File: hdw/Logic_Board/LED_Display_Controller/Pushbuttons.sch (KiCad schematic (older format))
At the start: 21 parts, among them J1401 Encoder Ext, SW1401 Display Enable, SW1402 Brightness/Enable, U1401 MAX6816, U1402 74LVC2G14, U1403 74LVC1G79

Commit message: added ESP8266 custom footprint
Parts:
- SW1402: footprint (none) -> Electronic_Display_Footprint_Lib:ACZ11BR4E-15FA1-20C
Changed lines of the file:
@@
 F 0 "SW1402" H 1970 4750 50  0000 C CNN
 F 1 "Brightness/Enable" H 1970 4230 50  0000 C CNN
-F 2 "" H 1820 4650 50  0001 C CNN
+F 2 "Electronic_Display_Footprint_Lib:ACZ11BR4E-15FA1-20C" H 1820 4650 50  0001 C CNN
 F 3 "~" H 1970 4750 50  0001 C CNN
 	1    1970 4490

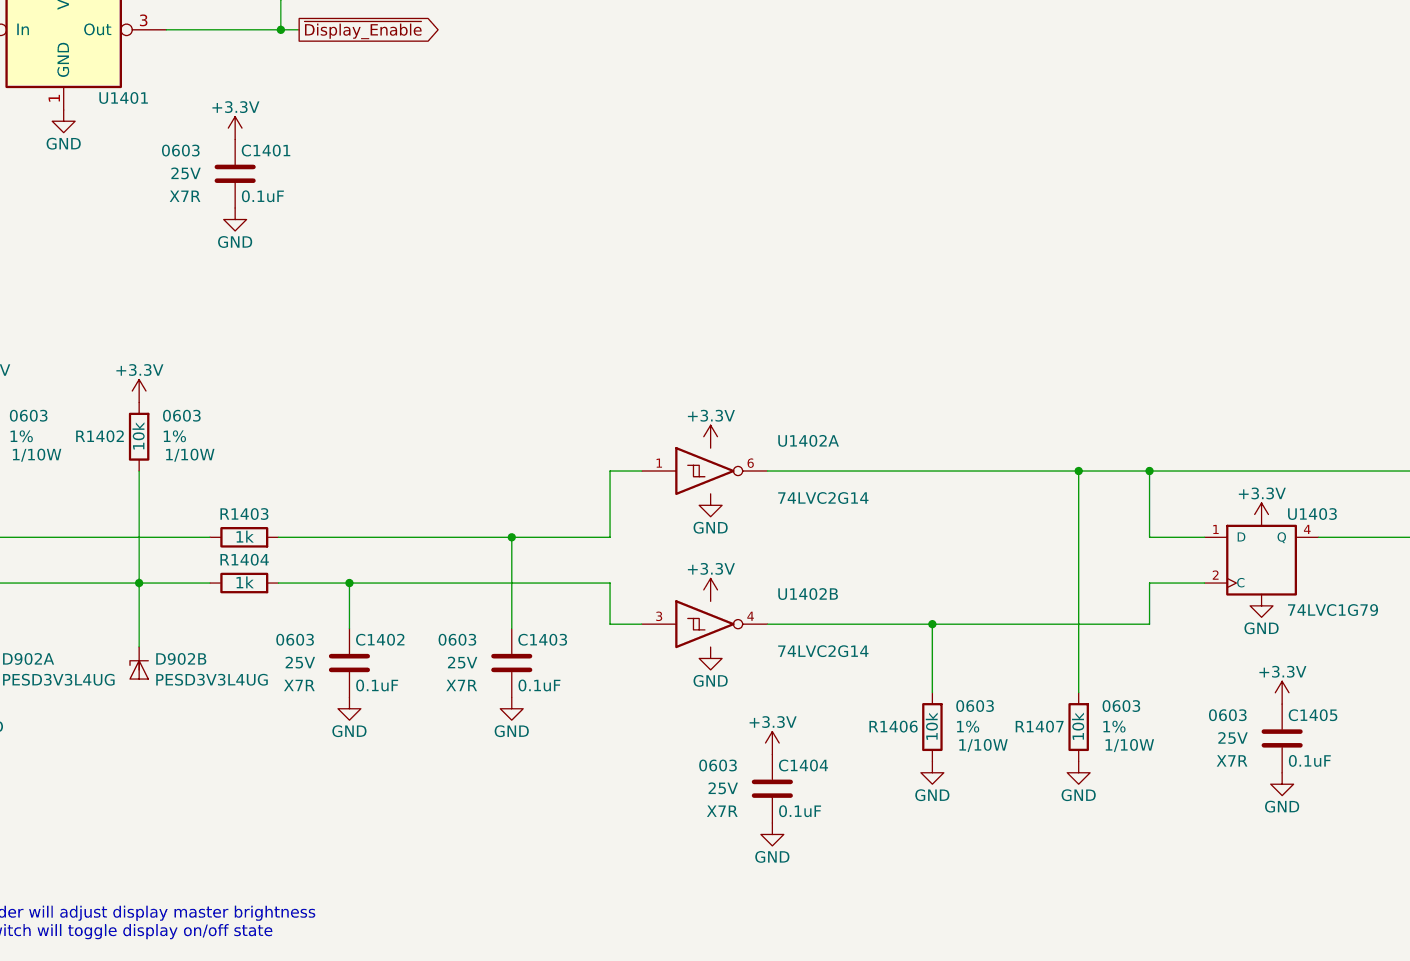
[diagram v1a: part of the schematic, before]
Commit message: Added some digikey partnumbers to components
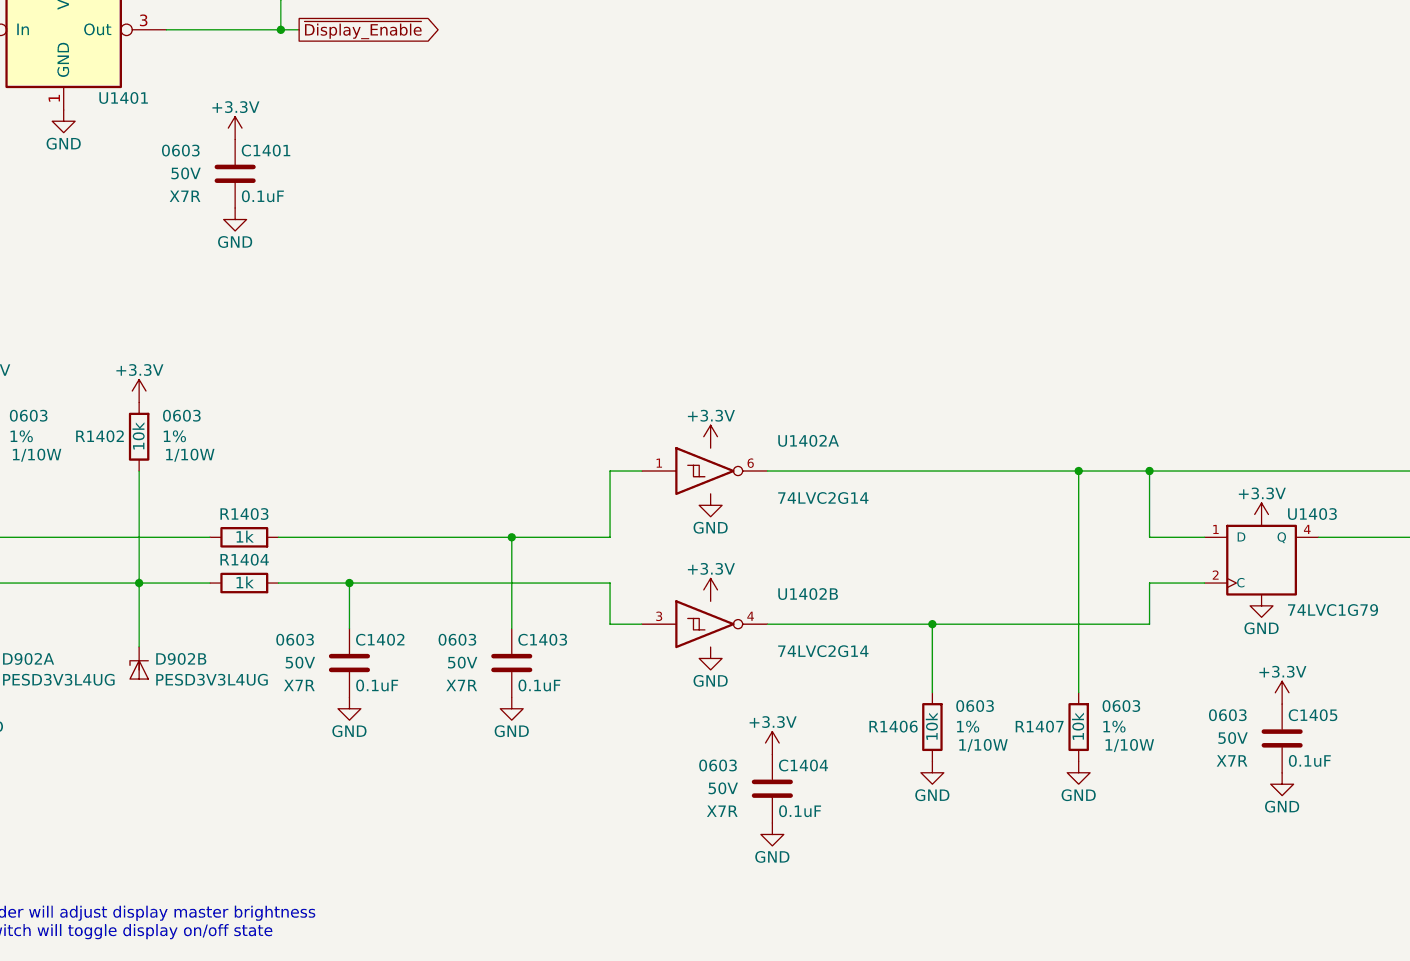
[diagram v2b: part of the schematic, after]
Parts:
- C1401, C1402, C1403, C1404, C1405: footprint (none) -> Capacitors_SMD:C_0603; Digi-Key PN PN -> 311-1344-1-ND; Voltage 25V -> 50V
- D1401, D902: Digi-Key PN (none) -> 1727-3827-1-ND
- SW1402: Digi-Key PN (none) -> 102-1753-ND
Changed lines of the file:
@@
 F 2 "Electronic_Display_Footprint_Lib:ACZ11BR4E-15FA1-20C" H 1820 4650 50  0001 C CNN
 F 3 "~" H 1970 4750 50  0001 C CNN
+F 4 "102-1753-ND" H 0   0   50  0001 C CNN "Digi-Key PN"
 	1    1970 4490
 	-1   0    0    -1
@@
 F 0 "C1401" H 4205 2900 50  0000 L CNN
 F 1 "0.1uF" H 4205 2700 50  0000 L CNN
-F 2 "" H 4218 2650 50  0001 C CNN
+F 2 "Capacitors_SMD:C_0603" H 4218 2650 50  0001 C CNN
 F 3 "" H 4205 2900 50  0001 C CNN
 F 4 "0603" H 4030 2900 50  0000 R CNN "display_footprint"
-F 5 "25V" H 4030 2800 50  0000 R CNN "Voltage"
+F 5 "50V" H 4030 2800 50  0000 R CNN "Voltage"
 F 6 "X7R" H 4030 2700 50  0000 R CNN "Dielectric"
-F 7 "PN" H 4605 3300 60  0001 C CNN "Digi-Key PN"
+F 7 "311-1344-1-ND" H 4605 3300 60  0001 C CNN "Digi-Key PN"
 	1    4180 2800
 	1    0    0    -1
@@
 F 0 "C1402" H 4705 5040 50  0000 L CNN
 F 1 "0.1uF" H 4705 4840 50  0000 L CNN
-F 2 "" H 4718 4790 50  0001 C CNN
+F 2 "Capacitors_SMD:C_0603" H 4718 4790 50  0001 C CNN
 F 3 "" H 4705 5040 50  0001 C CNN
 F 4 "0603" H 4530 5040 50  0000 R CNN "display_footprint"
-F 5 "25V" H 4530 4940 50  0000 R CNN "Voltage"
+F 5 "50V" H 4530 4940 50  0000 R CNN "Voltage"
 F 6 "X7R" H 4530 4840 50  0000 R CNN "Dielectric"
-F 7 "PN" H 5105 5440 60  0001 C CNN "Digi-Key PN"
+F 7 "311-1344-1-ND" H 5105 5440 60  0001 C CNN "Digi-Key PN"
 	1    4680 4940
 	1    0    0    -1
@@
 F 0 "C1403" H 5415 5040 50  0000 L CNN
 F 1 "0.1uF" H 5415 4840 50  0000 L CNN
-F 2 "" H 5428 4790 50  0001 C CNN
+F 2 "Capacitors_SMD:C_0603" H 5428 4790 50  0001 C CNN
 F 3 "" H 5415 5040 50  0001 C CNN
 F 4 "0603" H 5240 5040 50  0000 R CNN "display_footprint"
-F 5 "25V" H 5240 4940 50  0000 R CNN "Voltage"
+F 5 "50V" H 5240 4940 50  0000 R CNN "Voltage"
 F 6 "X7R" H 5240 4840 50  0000 R CNN "Dielectric"
-F 7 "PN" H 5815 5440 60  0001 C CNN "Digi-Key PN"
+F 7 "311-1344-1-ND" H 5815 5440 60  0001 C CNN "Digi-Key PN"
 	1    5390 4940
 	1    0    0    -1
@@
 F 0 "C1404" H 6555 5590 50  0000 L CNN
 F 1 "0.1uF" H 6555 5390 50  0000 L CNN
-F 2 "" H 6568 5340 50  0001 C CNN
+F 2 "Capacitors_SMD:C_0603" H 6568 5340 50  0001 C CNN
 F 3 "" H 6555 5590 50  0001 C CNN
 F 4 "0603" H 6380 5590 50  0000 R CNN "display_footprint"
-F 5 "25V" H 6380 5490 50  0000 R CNN "Voltage"
+F 5 "50V" H 6380 5490 50  0000 R CNN "Voltage"
 F 6 "X7R" H 6380 5390 50  0000 R CNN "Dielectric"
-F 7 "PN" H 6955 5990 60  0001 C CNN "Digi-Key PN"
+F 7 "311-1344-1-ND" H 6955 5990 60  0001 C CNN "Digi-Key PN"
 	1    6530 5490
 	1    0    0    -1
@@
 F 0 "C1405" H 8785 5370 50  0000 L CNN
 F 1 "0.1uF" H 8785 5170 50  0000 L CNN
-F 2 "" H 8798 5120 50  0001 C CNN
+F 2 "Capacitors_SMD:C_0603" H 8798 5120 50  0001 C CNN
 F 3 "" H 8785 5370 50  0001 C CNN
 F 4 "0603" H 8610 5370 50  0000 R CNN "display_footprint"
-F 5 "25V" H 8610 5270 50  0000 R CNN "Voltage"
+F 5 "50V" H 8610 5270 50  0000 R CNN "Voltage"
 F 6 "X7R" H 8610 5170 50  0000 R CNN "Dielectric"
-F 7 "PN" H 9185 5770 60  0001 C CNN "Digi-Key PN"
+F 7 "311-1344-1-ND" H 9185 5770 60  0001 C CNN "Digi-Key PN"
 	1    8760 5270
 	1    0    0    -1
@@
 F 2 "Package_TO_SOT_SMD:SOT-353_SC-70-5" H 3090 4970 50  0001 C CNN
 F 3 "http://www.nxp.com/documents/data_sheet/PESDXL4UF_G_W.pdf" H 3090 4970 50  0001 C CNN
+F 4 "1727-3827-1-ND" H 0   0   50  0001 C CNN "Digi-Key PN"
 	1    3090 4970
 	0    1    1    0
@@
 F 2 "Package_TO_SOT_SMD:SOT-353_SC-70-5" H 3760 4970 50  0001 C CNN
 F 3 "http://www.nxp.com/documents/data_sheet/PESDXL4UF_G_W.pdf" H 3760 4970 50  0001 C CNN
+F 4 "1727-3827-1-ND" H 0   0   50  0001 C CNN "Digi-Key PN"
 	2    3760 4970
 	0    1    1    0
@@
 F 2 "Package_TO_SOT_SMD:SOT-353_SC-70-5" H 2010 2420 50  0001 C CNN
 F 3 "http://www.nxp.com/documents/data_sheet/PESDXL4UF_G_W.pdf" H 2010 2420 50  0001 C CNN
+F 4 "1727-3827-1-ND" H 0   0   50  0001 C CNN "Digi-Key PN"
 	3    2010 2420
 	0    1    1    0

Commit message: Finished first pass of digikey part numbers
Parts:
- R1401, R1402, R1405, R1406, R1407, R1408: Digi-Key PN PN -> RMCF0603FT10K0CT-ND
- R1403, R1404: Digi-Key PN PN -> RMCF0603FT1K00CT-ND
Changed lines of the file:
@@
 F 5 "1%" H 4480 1890 50  0000 L CNN "Tolerance"
 F 6 "1/10W" H 4490 1810 50  0000 L CNN "Wattage"
-F 7 "PN" H 4680 2290 60  0001 C CNN "Digi-Key PN"
+F 7 "RMCF0603FT10K0CT-ND" H 4680 2290 60  0001 C CNN "Digi-Key PN"
 	1    4380 1890
 	1    0    0    -1
@@
 F 5 "1%" H 3190 3950 50  0000 L CNN "Tolerance"
 F 6 "1/10W" H 3200 3870 50  0000 L CNN "Wattage"
-F 7 "PN" H 3390 4350 60  0001 C CNN "Digi-Key PN"
+F 7 "RMCF0603FT10K0CT-ND" H 3390 4350 60  0001 C CNN "Digi-Key PN"
 	1    3090 3950
 	1    0    0    -1
@@
 F 5 "1%" H 3860 3950 50  0000 L CNN "Tolerance"
 F 6 "1/10W" H 3870 3870 50  0000 L CNN "Wattage"
-F 7 "PN" H 4060 4350 60  0001 C CNN "Digi-Key PN"
+F 7 "RMCF0603FT10K0CT-ND" H 4060 4350 60  0001 C CNN "Digi-Key PN"
 	1    3760 3950
 	1    0    0    -1
@@
 F 2 "" H 4220 4390 50  0001 C CNN
 F 3 "" H 4220 4390 50  0001 C CNN
-F 4 "PN" H 4520 4790 60  0001 C CNN "Digi-Key PN"
+F 4 "RMCF0603FT1K00CT-ND" H 4520 4790 60  0001 C CNN "Digi-Key PN"
 F 5 "0603" V 4320 4390 50  0001 C CNN "display_footprint"
 F 6 "1%" V 4420 4390 50  0001 C CNN "Tolerance"
@@
 F 2 "" H 4220 4590 50  0001 C CNN
 F 3 "" H 4220 4590 50  0001 C CNN
-F 4 "PN" H 4520 4990 60  0001 C CNN "Digi-Key PN"
+F 4 "RMCF0603FT1K00CT-ND" H 4520 4990 60  0001 C CNN "Digi-Key PN"
 F 5 "0603" V 4320 4590 50  0001 C CNN "display_footprint"
 F 6 "1%" V 4420 4590 50  0001 C CNN "Tolerance"
@@
 F 5 "1%" H 7330 5220 50  0000 L CNN "Tolerance"
 F 6 "1/10W" H 7340 5140 50  0000 L CNN "Wattage"
-F 7 "PN" H 7530 5620 60  0001 C CNN "Digi-Key PN"
+F 7 "RMCF0603FT10K0CT-ND" H 7530 5620 60  0001 C CNN "Digi-Key PN"
 	1    7230 5220
 	1    0    0    -1
@@
 F 5 "1%" H 7970 5220 50  0000 L CNN "Tolerance"
 F 6 "1/10W" H 7980 5140 50  0000 L CNN "Wattage"
-F 7 "PN" H 8170 5620 60  0001 C CNN "Digi-Key PN"
+F 7 "RMCF0603FT10K0CT-ND" H 8170 5620 60  0001 C CNN "Digi-Key PN"
 	1    7870 5220
 	1    0    0    -1
@@
 F 5 "1%" H 9700 4660 50  0000 L CNN "Tolerance"
 F 6 "1/10W" H 9710 4580 50  0000 L CNN "Wattage"
-F 7 "PN" H 9900 5060 60  0001 C CNN "Digi-Key PN"
+F 7 "RMCF0603FT10K0CT-ND" H 9900 5060 60  0001 C CNN "Digi-Key PN"
 	1    9600 4660
 	1    0    0    -1

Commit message: First pass assignment of footprints to all components
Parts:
- D1401: footprint Package_TO_SOT_SMD:SOT-353_SC-70-5 -> TO_SOT_Packages_SMD:SOT-353_SC-70-5
- J1401: footprint (none) -> Pin_Headers:Pin_Header_Straight_1x05_Pitch2.54mm
- R1401, R1402, R1403, R1404, R1405, R1406, R1407, R1408: footprint (none) -> Resistors_SMD:R_0603
- SW1401: footprint (none) -> Buttons_Switches_THT:SW_PUSH_6mm
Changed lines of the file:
@@
 F 0 "SW1401" H 1310 2455 50  0000 C CNN
 F 1 "Display Enable" H 1310 2364 50  0000 C CNN
-F 2 "" H 1310 2370 50  0001 C CNN
+F 2 "Buttons_Switches_THT:SW_PUSH_6mm" H 1310 2370 50  0001 C CNN
 F 3 "" H 1310 2370 50  0001 C CNN
 	1    1310 2170
@@
 F 0 "R1405" H 4320 1890 50  0000 R CNN
 F 1 "10k" V 4380 1890 50  0000 C CNN
-F 2 "" H 4380 1890 50  0001 C CNN
+F 2 "Resistors_SMD:R_0603" H 4380 1890 50  0001 C CNN
 F 3 "" H 4380 1890 50  0001 C CNN
 F 4 "0603" H 4480 1980 50  0000 L CNN "display_footprint"
@@
 F 0 "R1401" H 3030 3950 50  0000 R CNN
 F 1 "10k" V 3090 3950 50  0000 C CNN
-F 2 "" H 3090 3950 50  0001 C CNN
+F 2 "Resistors_SMD:R_0603" H 3090 3950 50  0001 C CNN
 F 3 "" H 3090 3950 50  0001 C CNN
 F 4 "0603" H 3190 4040 50  0000 L CNN "display_footprint"
@@
 F 0 "R1402" H 3700 3950 50  0000 R CNN
 F 1 "10k" V 3760 3950 50  0000 C CNN
-F 2 "" H 3760 3950 50  0001 C CNN
+F 2 "Resistors_SMD:R_0603" H 3760 3950 50  0001 C CNN
 F 3 "" H 3760 3950 50  0001 C CNN
 F 4 "0603" H 3860 4040 50  0000 L CNN "display_footprint"
@@
 F 0 "R1403" V 4120 4390 50  0000 C CNN
 F 1 "1k" V 4220 4390 50  0000 C CNN
-F 2 "" H 4220 4390 50  0001 C CNN
+F 2 "Resistors_SMD:R_0603" H 4220 4390 50  0001 C CNN
 F 3 "" H 4220 4390 50  0001 C CNN
 F 4 "RMCF0603FT1K00CT-ND" H 4520 4790 60  0001 C CNN "Digi-Key PN"
@@
 F 0 "R1404" V 4120 4590 50  0000 C CNN
 F 1 "1k" V 4220 4590 50  0000 C CNN
-F 2 "" H 4220 4590 50  0001 C CNN
+F 2 "Resistors_SMD:R_0603" H 4220 4590 50  0001 C CNN
 F 3 "" H 4220 4590 50  0001 C CNN
 F 4 "RMCF0603FT1K00CT-ND" H 4520 4990 60  0001 C CNN "Digi-Key PN"
@@
 F 0 "R1406" H 7170 5220 50  0000 R CNN
 F 1 "10k" V 7230 5220 50  0000 C CNN
-F 2 "" H 7230 5220 50  0001 C CNN
+F 2 "Resistors_SMD:R_0603" H 7230 5220 50  0001 C CNN
 F 3 "" H 7230 5220 50  0001 C CNN
 F 4 "0603" H 7330 5310 50  0000 L CNN "display_footprint"
@@
 F 0 "R1407" H 7810 5220 50  0000 R CNN
 F 1 "10k" V 7870 5220 50  0000 C CNN
-F 2 "" H 7870 5220 50  0001 C CNN
+F 2 "Resistors_SMD:R_0603" H 7870 5220 50  0001 C CNN
 F 3 "" H 7870 5220 50  0001 C CNN
 F 4 "0603" H 7970 5310 50  0000 L CNN "display_footprint"
@@
 F 0 "R1408" H 9540 4660 50  0000 R CNN
 F 1 "10k" V 9600 4660 50  0000 C CNN
-F 2 "" H 9600 4660 50  0001 C CNN
+F 2 "Resistors_SMD:R_0603" H 9600 4660 50  0001 C CNN
 F 3 "" H 9600 4660 50  0001 C CNN
 F 4 "0603" H 9700 4750 50  0000 L CNN "display_footprint"
@@
 F 0 "D1401" V 1964 2488 50  0000 L CNN
 F 1 "PESD3V3L4UG" V 2055 2488 50  0000 L CNN
-F 2 "Package_TO_SOT_SMD:SOT-353_SC-70-5" H 2010 2420 50  0001 C CNN
+F 2 "TO_SOT_Packages_SMD:SOT-353_SC-70-5" H 2010 2420 50  0001 C CNN
 F 3 "http://www.nxp.com/documents/data_sheet/PESDXL4UF_G_W.pdf" H 2010 2420 50  0001 C CNN
 F 4 "1727-3827-1-ND" H 0   0   50  0001 C CNN "Digi-Key PN"
@@
 F 0 "J1401" H 1110 3520 50  0000 L CNN
 F 1 "Encoder Ext" H 1120 3440 50  0000 L CNN
-F 2 "" H 1040 3530 50  0001 C CNN
+F 2 "Pin_Headers:Pin_Header_Straight_1x05_Pitch2.54mm" H 1040 3530 50  0001 C CNN
 F 3 "~" H 1040 3530 50  0001 C CNN
 	1    1040 3530

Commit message: Resolved a few library dependencies
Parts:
- D902: footprint Package_TO_SOT_SMD:SOT-353_SC-70-5 -> TO_SOT_Packages_SMD:SOT-353_SC-70-5
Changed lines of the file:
@@
 F 0 "D902" V 3044 5038 50  0000 L CNN
 F 1 "PESD3V3L4UG" V 3135 5038 50  0000 L CNN
-F 2 "Package_TO_SOT_SMD:SOT-353_SC-70-5" H 3090 4970 50  0001 C CNN
+F 2 "TO_SOT_Packages_SMD:SOT-353_SC-70-5" H 3090 4970 50  0001 C CNN
 F 3 "http://www.nxp.com/documents/data_sheet/PESDXL4UF_G_W.pdf" H 3090 4970 50  0001 C CNN
 F 4 "1727-3827-1-ND" H 0   0   50  0001 C CNN "Digi-Key PN"
@@
 F 0 "D902" V 3714 5038 50  0000 L CNN
 F 1 "PESD3V3L4UG" V 3805 5038 50  0000 L CNN
-F 2 "Package_TO_SOT_SMD:SOT-353_SC-70-5" H 3760 4970 50  0001 C CNN
+F 2 "TO_SOT_Packages_SMD:SOT-353_SC-70-5" H 3760 4970 50  0001 C CNN
 F 3 "http://www.nxp.com/documents/data_sheet/PESDXL4UF_G_W.pdf" H 3760 4970 50  0001 C CNN
 F 4 "1727-3827-1-ND" H 0   0   50  0001 C CNN "Digi-Key PN"

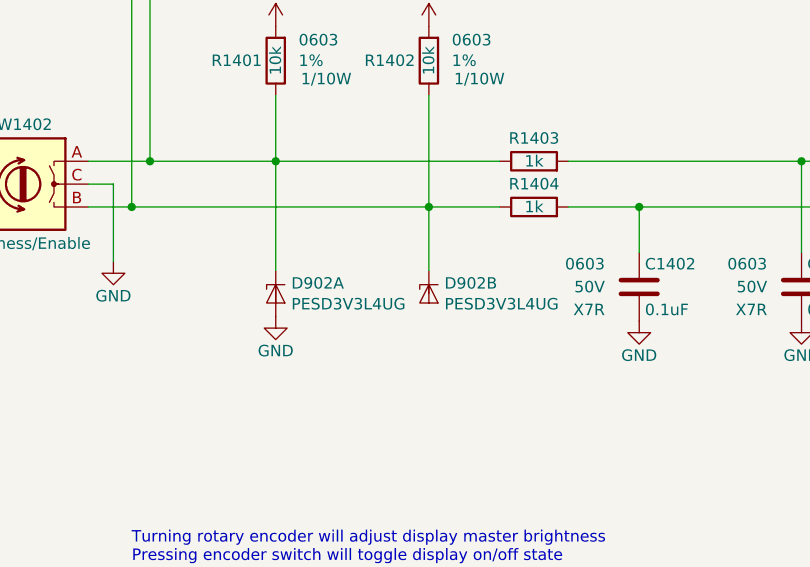
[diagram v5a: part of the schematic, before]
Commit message: Placed decoupling caps around micro
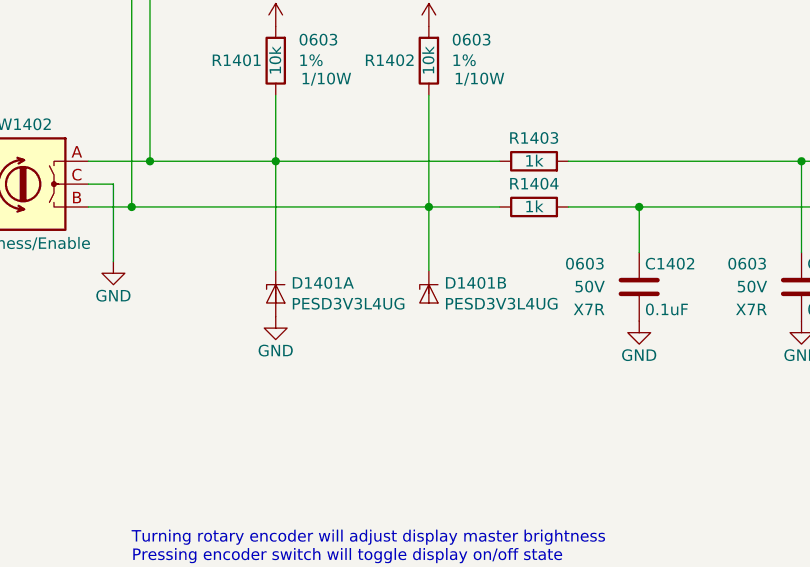
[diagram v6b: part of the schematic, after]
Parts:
- renumbered D902 to D1401
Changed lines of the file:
@@
 Connection ~ 8180 4100
 $Comp
-L Power_Protection:PESD3V3L4UG D902
+L Power_Protection:PESD3V3L4UG D1401
 U 1 1 5BF48679
 P 3090 4970
-F 0 "D902" V 3044 5038 50  0000 L CNN
+F 0 "D1401" V 3044 5038 50  0000 L CNN
 F 1 "PESD3V3L4UG" V 3135 5038 50  0000 L CNN
 F 2 "TO_SOT_Packages_SMD:SOT-353_SC-70-5" H 3090 4970 50  0001 C CNN
@@
 $EndComp
 $Comp
-L Power_Protection:PESD3V3L4UG D902
+L Power_Protection:PESD3V3L4UG D1401
 U 2 1 5BF4A271
 P 3760 4970
-F 0 "D902" V 3714 5038 50  0000 L CNN
+F 0 "D1401" V 3714 5038 50  0000 L CNN
 F 1 "PESD3V3L4UG" V 3805 5038 50  0000 L CNN
 F 2 "TO_SOT_Packages_SMD:SOT-353_SC-70-5" H 3760 4970 50  0001 C CNN

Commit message: Resolved pinout issue with TVS diodes
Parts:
- D1401: symbol Power_Protection:PESD3V3L4UG -> LED_Display_Local_Library:PESD3V3L4UG
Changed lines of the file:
@@
 Connection ~ 8180 4100
 $Comp
-L Power_Protection:PESD3V3L4UG D1401
+L LED_Display_Local_Library:PESD3V3L4UG D1401
 U 1 1 5BF48679
 P 3090 4970
@@
 $EndComp
 $Comp
-L Power_Protection:PESD3V3L4UG D1401
+L LED_Display_Local_Library:PESD3V3L4UG D1401
 U 2 1 5BF4A271
 P 3760 4970
@@
 	3090 4870 3090 4390
 $Comp
-L Power_Protection:PESD3V3L4UG D1401
+L LED_Display_Local_Library:PESD3V3L4UG D1401
 U 3 1 5BF61551
 P 2010 2420
